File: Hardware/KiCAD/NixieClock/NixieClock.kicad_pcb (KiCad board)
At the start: 2 copper layers, 236.2 x 61 mm, 18 parts, among them IC1 , IC2 

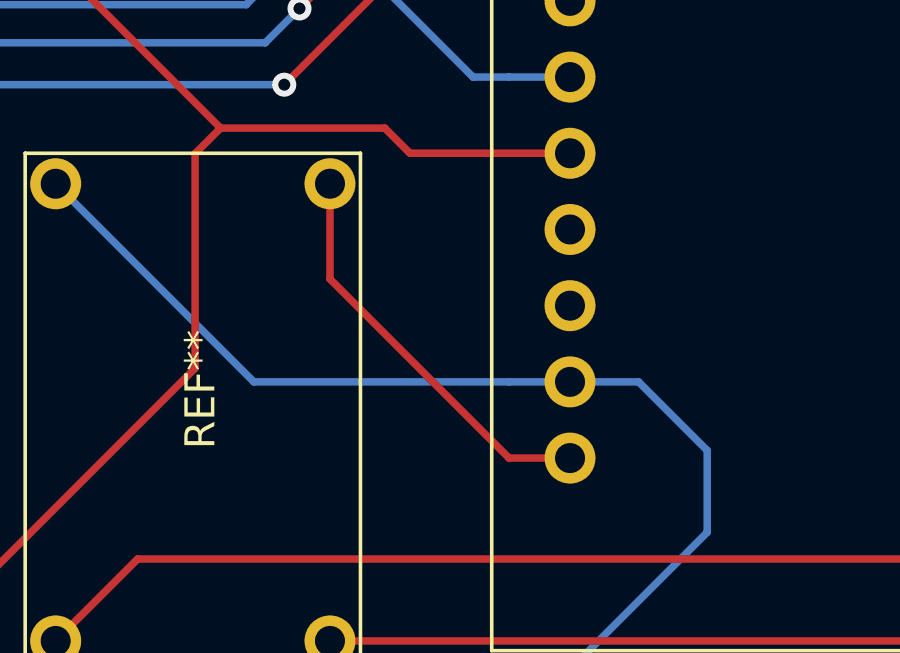
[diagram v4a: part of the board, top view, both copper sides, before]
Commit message: Added Vin Diode
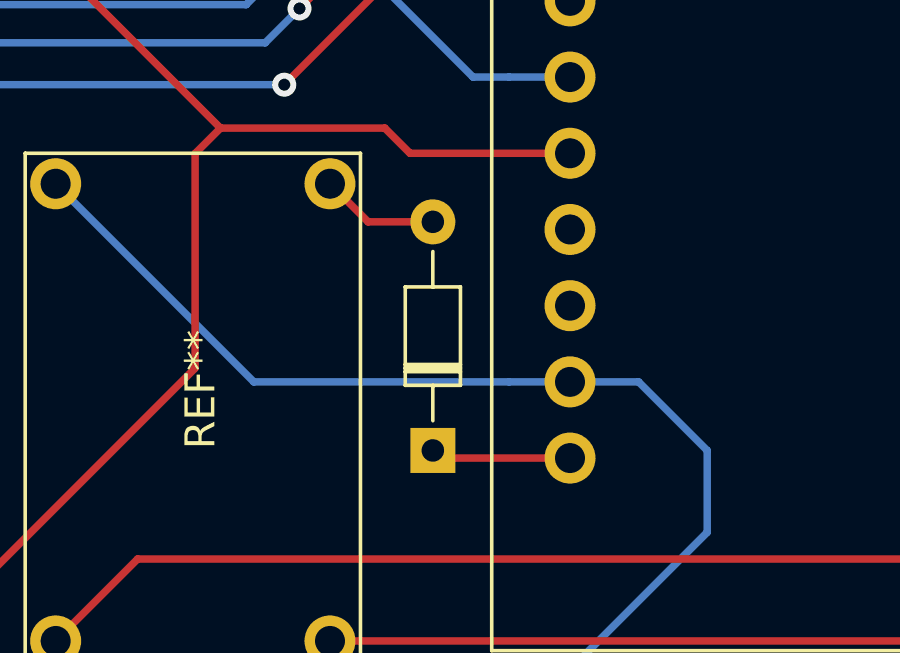
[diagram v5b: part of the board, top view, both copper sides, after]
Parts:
- added  : , Diode_THT:D_DO-34_SOD68_P7.62mm_Horizontal, F.Cu at (235.7, 124.0)
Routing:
- net (no net): track 3296.5 -> 3291.5 mm
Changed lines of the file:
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@@
     (thickness 1.6)
     (drawings 6)
-    (tracks 499)
+    (tracks 500)
     (zones 0)
-    (modules 18)
+    (modules 19)
     (nets 1)
   )
@@
     (uvia_dia 0.3)
     (uvia_drill 0.1)
+  )
+  (module Diode_THT:D_DO-34_SOD68_P7.62mm_Horizontal (layer F.Cu)
+    (at 235.712 123.952 90)
+    (descr "Diode, DO-34_SOD68 series, Axial, Horizontal, pin pitch=7.62mm, , length*diameter=3.04*1.6mm^2, , https://www.nxp.com/docs/en/data-sheet/KTY83_SER.pdf")
+    (tags "Diode DO-34_SOD68 series Axial Horizontal pin pitch 7.62mm  length 3.04mm diameter 1.6mm")
+    (fp_text reference " " (at 3.81 -1.92 90) (layer F.SilkS)
+      (effects (font (size 1 1) (thickness 0.15)))
+    )
+    (fp_text value " " (at 3.81 1.92 90) (layer F.Fab)
+      (effects (font (size 1 1) (thickness 0.15)))
+    )
+    (fp_text user " " (at 0 -1.75 90) (layer F.Fab)
+      (effects (font (size 1 1) (thickness 0.15)))
+    )
+    (fp_text user %R (at 4.038 0 270) (layer F.Fab)
+      (effects (font (size 0.608 0.608) (thickness 0.0912)))
+    )
+    (fp_line (start 8.63 -1.05) (end -1 -1.05) (layer F.CrtYd) (width 0.05))
+    (fp_line (start 8.63 1.05) (end 8.63 -1.05) (layer F.CrtYd) (width 0.05))
+    (fp_line (start -1 1.05) (end 8.63 1.05) (layer F.CrtYd) (width 0.05))
+    (fp_line (start -1 -1.05) (end -1 1.05) (layer F.CrtYd) (width 0.05))
+    (fp_line (start 2.626 -0.92) (end 2.626 0.92) (layer F.SilkS) (width 0.12))
+    (fp_line (start 2.866 -0.92) (end 2.866 0.92) (layer F.SilkS) (width 0.12))
+    (fp_line (start 2.746 -0.92) (end 2.746 0.92) (layer F.SilkS) (width 0.12))
+    (fp_line (start 6.63 0) (end 5.45 0) (layer F.SilkS) (width 0.12))
+    (fp_line (start 0.99 0) (end 2.17 0) (layer F.SilkS) (width 0.12))
+    (fp_line (start 5.45 -0.92) (end 2.17 -0.92) (layer F.SilkS) (width 0.12))
+    (fp_line (start 5.45 0.92) (end 5.45 -0.92) (layer F.SilkS) (width 0.12))
+    (fp_line (start 2.17 0.92) (end 5.45 0.92) (layer F.SilkS) (width 0.12))
+    (fp_line (start 2.17 -0.92) (end 2.17 0.92) (layer F.SilkS) (width 0.12))
+    (fp_line (start 2.646 -0.8) (end 2.646 0.8) (layer F.Fab) (width 0.1))
+    (fp_line (start 2.846 -0.8) (end 2.846 0.8) (layer F.Fab) (width 0.1))
+    (fp_line (start 2.746 -0.8) (end 2.746 0.8) (layer F.Fab) (width 0.1))
+    (fp_line (start 7.62 0) (end 5.33 0) (layer F.Fab) (width 0.1))
+    (fp_line (start 0 0) (end 2.29 0) (layer F.Fab) (width 0.1))
+    (fp_line (start 5.33 -0.8) (end 2.29 -0.8) (layer F.Fab) (width 0.1))
+    (fp_line (start 5.33 0.8) (end 5.33 -0.8) (layer F.Fab) (width 0.1))
+    (fp_line (start 2.29 0.8) (end 5.33 0.8) (layer F.Fab) (width 0.1))
+    (fp_line (start 2.29 -0.8) (end 2.29 0.8) (layer F.Fab) (width 0.1))
+    (pad 2 thru_hole oval (at 7.62 0 90) (size 1.5 1.5) (drill 0.75) (layers *.Cu *.Mask))
+    (pad 1 thru_hole rect (at 0 0 90) (size 1.5 1.5) (drill 0.75) (layers *.Cu *.Mask))
+    (model ${KISYS3DMOD}/Diode_THT.3dshapes/D_DO-34_SOD68_P7.62mm_Horizontal.wrl
+      (at (xyz 0 0 0))
+      (scale (xyz 1 1 1))
+      (rotate (xyz 0 0 0))
+    )
   )
   (module NixieClock:NCH6100HV (layer F.Cu)
@@
   (segment (start 194.1703 79.3242) (end 219.9513 79.3242) (width 0.25) (layer F.Cu) (net 0))
   (segment (start 219.9513 79.3242) (end 268.4526 79.3242) (width 0.25) (layer F.Cu) (net 0))
-  (segment (start 232.283 118.237) (end 238.252 124.206) (width 0.25) (layer F.Cu) (net 0))
-  (segment (start 232.283 115.062) (end 232.283 118.237) (width 0.25) (layer F.Cu) (net 0))
   (segment (start 225.8695 127.5715) (end 223.139 130.302) (width 0.25) (layer F.Cu) (net 0))
   (segment (start 237.049919 111.506) (end 233.807 108.263081) (width 0.25) (layer B.Cu) (net 0))
@@
   (segment (start 263.144 93.726) (end 261.112 93.726) (width 0.25) (layer F.Cu) (net 0))
   (segment (start 238.252 111.506) (end 240.284 111.506) (width 0.25) (layer B.Cu) (net 0))
-  (segment (start 238.252 124.206) (end 240.284 124.206) (width 0.25) (layer F.Cu) (net 0))
   (segment (start 262.7275 127.5715) (end 262.0645 127.5715) (width 0.25) (layer F.Cu) (net 0))
   (segment (start 272.897 117.402) (end 262.7275 127.5715) (width 0.25) (layer F.Cu) (net 0))
@@
   (segment (start 265.077 130.302) (end 277.977 117.402) (width 0.25) (layer F.Cu) (net 0))
   (segment (start 232.283 130.302) (end 265.077 130.302) (width 0.25) (layer F.Cu) (net 0))
+  (segment (start 235.966 124.206) (end 235.712 123.952) (width 0.25) (layer F.Cu) (net 0))
+  (segment (start 240.284 124.206) (end 235.966 124.206) (width 0.25) (layer F.Cu) (net 0))
+  (segment (start 233.553 116.332) (end 232.283 115.062) (width 0.25) (layer F.Cu) (net 0))
+  (segment (start 235.712 116.332) (end 233.553 116.332) (width 0.25) (layer F.Cu) (net 0))
 )

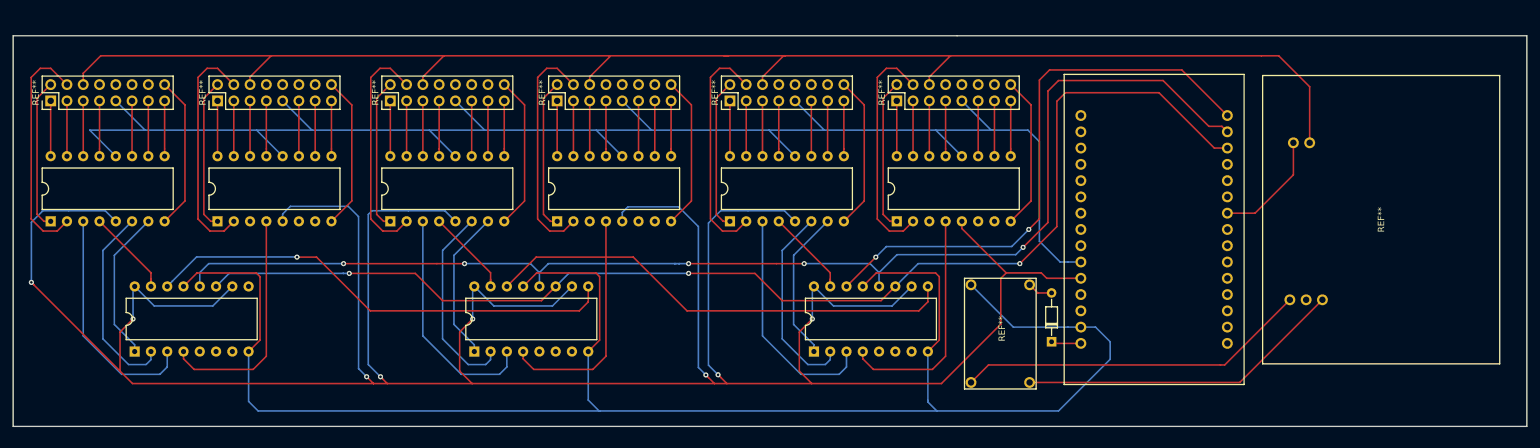
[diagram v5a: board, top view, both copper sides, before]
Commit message: Routed 3 buttons and resistors, routed dimming HW,
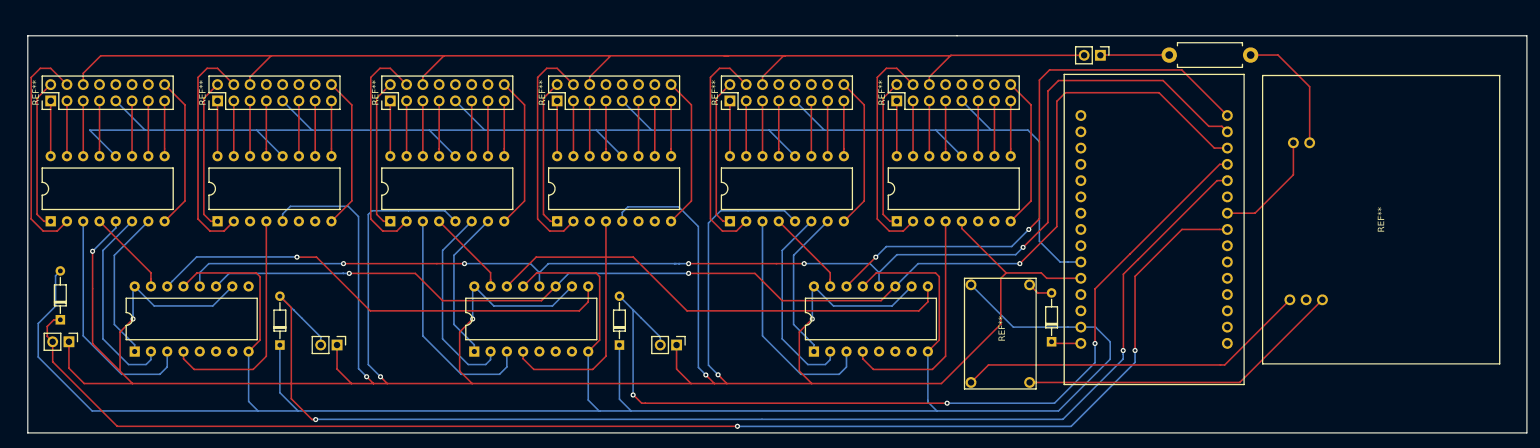
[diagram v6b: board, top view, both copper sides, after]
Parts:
- added  : , Connector_PinHeader_2.54mm:PinHeader_1x02_P2.54mm_Vertical, F.Cu at (243.3, 79.2)
- added  : , Diode_THT:D_DO-34_SOD68_P7.62mm_Horizontal, F.Cu at (81.0, 120.5)
- added  : , Connector_PinHeader_2.54mm:PinHeader_1x02_P2.54mm_Vertical, F.Cu at (82.4, 124.0)
- added  : , Diode_THT:D_DO-34_SOD68_P7.62mm_Horizontal, F.Cu at (115.3, 124.5)
- added  : , Connector_PinHeader_2.54mm:PinHeader_1x02_P2.54mm_Vertical, F.Cu at (124.2, 124.5)
- added  : , Connector_PinHeader_2.54mm:PinHeader_1x02_P2.54mm_Vertical, F.Cu at (177.2, 124.5)
- added  : , Diode_THT:D_DO-34_SOD68_P7.62mm_Horizontal, F.Cu at (168.3, 124.5)
- added  : , Resistor_THT:R_Axial_DIN0411_L9.9mm_D3.6mm_P12.70mm_Horizontal, F.Cu at (254.1, 79.2)
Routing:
- net (no net): track 3291.5 -> 3916.6 mm, vias 19 -> 26
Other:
- board size 236.2 x 61 mm -> 233.9 x 62 mm

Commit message: Routed all cathodes to RGB LEDs
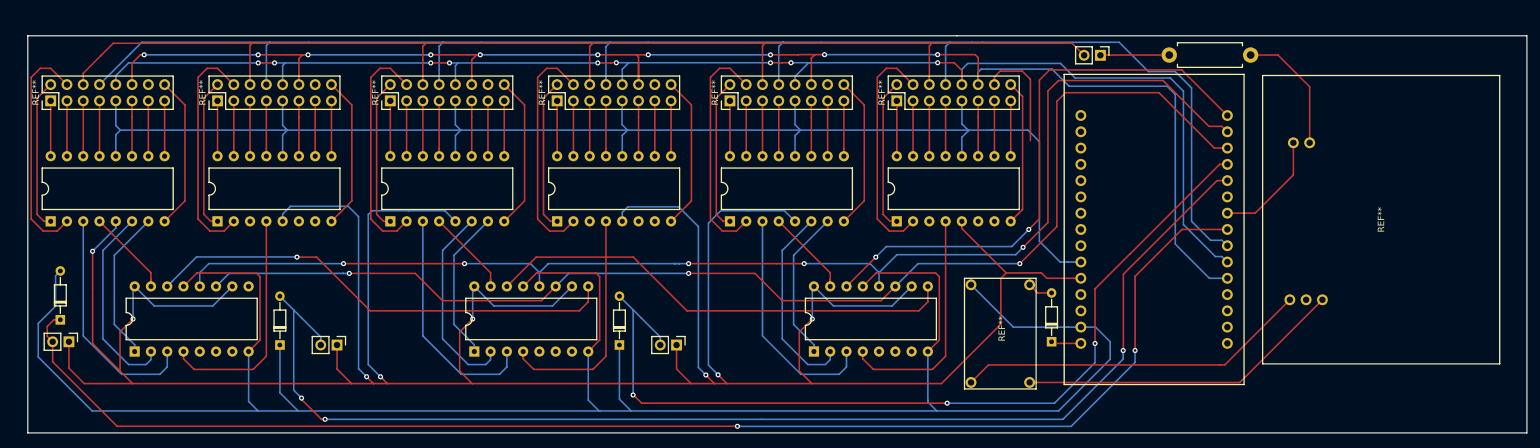
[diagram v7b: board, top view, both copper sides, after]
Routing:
- net (no net): track 3916.6 -> 4602.8 mm, vias 26 -> 46

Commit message: Routed holes for nixie tube resistors
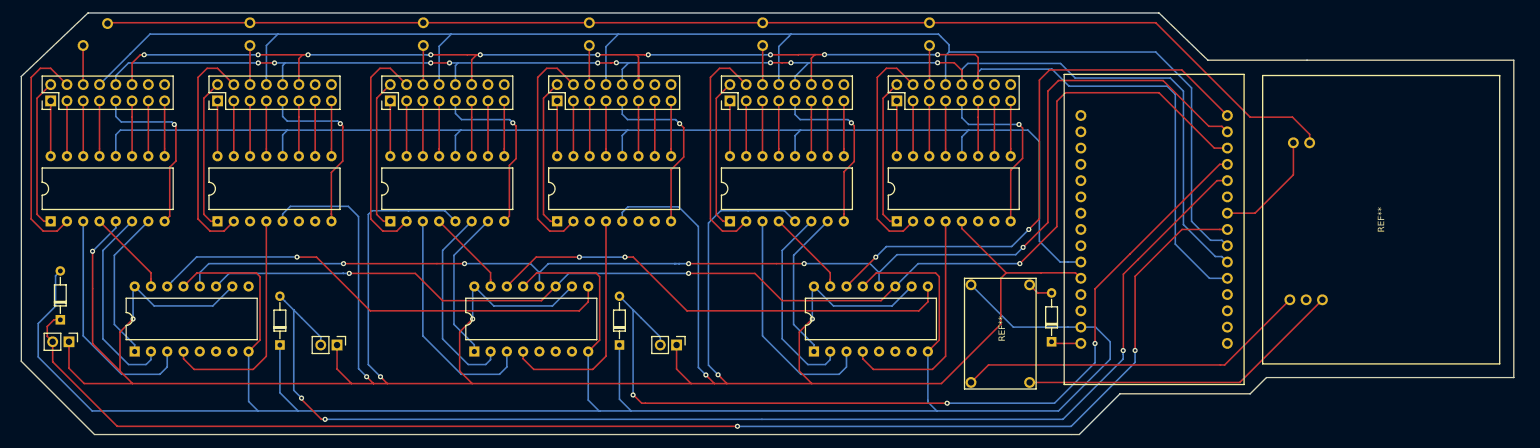
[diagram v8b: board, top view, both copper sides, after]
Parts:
- removed the   at (243.3, 79.2)
- removed the   at (254.1, 79.2)
- added  : , Connector_PinHeader_2.54mm:PinHeader_1x01_P2.54mm_Vertical, F.Cu at (84.6, 77.7)
- added  : , Connector_PinHeader_2.54mm:PinHeader_1x01_P2.54mm_Vertical, F.Cu at (190.6, 74.2)
- added  : , Connector_PinHeader_2.54mm:PinHeader_1x01_P2.54mm_Vertical, F.Cu at (216.7, 77.7)
- added  : , Connector_PinHeader_2.54mm:PinHeader_1x01_P2.54mm_Vertical, F.Cu at (216.7, 74.2)
- added  : , Connector_PinHeader_2.54mm:PinHeader_1x01_P2.54mm_Vertical, F.Cu at (88.4, 74.3)
- added  : , Connector_PinHeader_2.54mm:PinHeader_1x01_P2.54mm_Vertical, F.Cu at (110.6, 77.7)
- added  : , Connector_PinHeader_2.54mm:PinHeader_1x01_P2.54mm_Vertical, F.Cu at (110.6, 74.2)
- added  : , Connector_PinHeader_2.54mm:PinHeader_1x01_P2.54mm_Vertical, F.Cu at (137.7, 77.7)
- added  : , Connector_PinHeader_2.54mm:PinHeader_1x01_P2.54mm_Vertical, F.Cu at (137.7, 74.2)
- added  : , Connector_PinHeader_2.54mm:PinHeader_1x01_P2.54mm_Vertical, F.Cu at (163.6, 77.7)
- added  : , Connector_PinHeader_2.54mm:PinHeader_1x01_P2.54mm_Vertical, F.Cu at (163.6, 74.2)
- added  : , Connector_PinHeader_2.54mm:PinHeader_1x01_P2.54mm_Vertical, F.Cu at (190.6, 77.7)
-  : renamed from REF** (x6)
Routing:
- net (no net): track 4602.8 -> 4596.5 mm, vias 46 -> 54
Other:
- board size 233.9 x 62 mm -> 232.9 x 65.8 mm
